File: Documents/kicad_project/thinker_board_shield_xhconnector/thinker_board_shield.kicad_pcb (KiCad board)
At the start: 4 copper layers, 56 x 65 mm, 8 parts, among them J2 Thinker_board_S, U1 XH_S, U2 1PIN, U3 XH_4PIN

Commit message: add big wire /before auto-router
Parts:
- added U4: 2_pin, hoshina_library:2_pin, B.Cu at (40.6, 8.89)
- moved R1 5.79 mm to (27.8, 9.53)
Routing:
- net GND: track 73.9 -> 52.2 mm, vias 2 -> 1
- net +3V3: track 27.5 -> 9.54 mm
- net Net-(U2-Pad1): track 13.1 -> 0.00 mm, vias 1 -> 0
- net Net-(R1-Pad1): track 4.20 -> 0.00 mm
- net 5V: track 90.1 -> 87.7 mm
- removed copper zone on B.Cu, net GND
- removed copper zone on F.Cu, net GND
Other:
- board text added: "3.3V"
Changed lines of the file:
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@@
   (general
     (thickness 1.6)
-    (drawings 18)
-    (tracks 49)
+    (drawings 20)
+    (tracks 27)
     (zones 0)
-    (modules 8)
+    (modules 9)
     (nets 36)
   )
@@
   )
   (setup
-    (last_trace_width 0.16)
+    (last_trace_width 1)
     (user_trace_width 0.16)
     (user_trace_width 0.2)
@@
   )
   (module hoshina_library:register_0603 (layer F.Cu)
-    (at 29.718 14.986)
+    (at 27.79 9.525)
     (descr aitendo_R0603-1)
     (tags capacitor)
@@
     (pad "" np_thru_hole circle (at 0 0) (size 2.7 2.7) (drill 2.7) (layers *.Cu *.Mask))
   )
+  (module hoshina_library:2_pin (layer B.Cu)
+    (at 40.64 8.89 180)
+    (fp_text reference U4 (at 0 -3.675) (layer B.SilkS)
+      (effects (font (size 1 1) (thickness 0.15)) (justify mirror))
+    )
+    (fp_text value 2_pin (at 0 -2.675) (layer B.Fab)
+      (effects (font (size 1 1) (thickness 0.15)) (justify mirror))
+    )
+    (fp_line (start -2.54 1.27) (end 2.54 1.27) (layer B.CrtYd) (width 0.12))
+    (fp_line (start 2.54 1.27) (end 2.54 -1.27) (layer B.CrtYd) (width 0.12))
+    (fp_line (start 2.54 -1.27) (end -2.54 -1.27) (layer B.CrtYd) (width 0.12))
+    (fp_line (start -2.54 -1.27) (end -2.54 1.27) (layer B.CrtYd) (width 0.12))
+    (fp_line (start -1.397 1.524) (end -1.397 5.842) (layer B.Fab) (width 0.12))
+    (fp_line (start -1.397 5.842) (end -1.143 5.842) (layer B.Fab) (width 0.12))
+    (fp_line (start -1.143 5.842) (end -1.143 1.524) (layer B.Fab) (width 0.12))
+    (fp_line (start 1.143 1.524) (end 1.143 5.842) (layer B.Fab) (width 0.12))
+    (fp_line (start 1.397 5.842) (end 1.397 1.524) (layer B.Fab) (width 0.12))
+    (fp_line (start 1.143 5.842) (end 1.397 5.842) (layer B.Fab) (width 0.12))
+    (pad 1 thru_hole circle (at -1.27 0 180) (size 1.524 1.524) (drill 0.762) (layers *.Cu *.Mask)
+      (net 33 +3V3))
+    (pad 2 thru_hole circle (at 1.27 0 180) (size 1.524 1.524) (drill 0.762) (layers *.Cu *.Mask)
+      (net 32 GND))
+  )
+  (gr_text GND (at 39.37 1.27 90) (layer B.SilkS)
+    (effects (font (size 0.5 0.5) (thickness 0.1)) (justify mirror))
+  )
+  (gr_text 3.3V (at 41.91 1.27 90) (layer B.SilkS)
+    (effects (font (size 0.5 0.5) (thickness 0.1)) (justify mirror))
+  )
   (gr_arc (start 47 17.7) (end 48 17.7) (angle -90) (layer Edge.Cuts) (width 0.15))
   (gr_text sw2 (at 32.512 1.016 90) (layer B.SilkS)
@@
   (gr_line (start 0 3.5) (end 0 15.7) (layer Edge.Cuts) (width 0.15))
   (gr_line (start 3.5 0) (end 52.5 0) (layer Edge.Cuts) (width 0.15))
-  (segment (start 53.77 8.37) (end 53.77 7.5) (width 1.5) (layer B.Cu) (net 31))
-  (segment (start 53.77 7.5) (end 52.84 6.57) (width 1.5) (layer B.Cu) (net 31))
-  (segment (start 52.84 6.57) (end 41.4862 6.57) (width 1.5) (layer B.Cu) (net 31))
-  (segment (start 41.4862 6.57) (end 40.0742 5.158) (width 1.5) (layer B.Cu) (net 31))
-  (segment (start 40.0742 5.158) (end 18.342 5.158) (width 1.5) (layer B.Cu) (net 31))
-  (segment (start 18.342 5.158) (end 13 10.5) (width 1.5) (layer B.Cu) (net 31))
-  (segment (start 53.77 8.37) (end 53.77 7.1679) (width 1.5) (layer F.Cu) (net 31))
-  (segment (start 53.77 7.1679) (end 53.1721 6.57) (width 1.5) (layer F.Cu) (net 31))
-  (segment (start 53.1721 6.57) (end 41.7238 6.57) (width 1.5) (layer F.Cu) (net 31))
-  (segment (start 41.7238 6.57) (end 40.0578 4.904) (width 1.5) (layer F.Cu) (net 31))
-  (segment (start 40.0578 4.904) (end 18.596 4.904) (width 1.5) (layer F.Cu) (net 31))
-  (segment (start 18.596 4.904) (end 13 10.5) (width 1.5) (layer F.Cu) (net 31))
-  (segment (start 45.512 13) (end 45.7496 13) (width 1.5) (layer B.Cu) (net 32))
-  (segment (start 45.7496 13) (end 45.8388 13.0892) (width 1.5) (layer B.Cu) (net 32))
-  (segment (start 49.025 16.2754) (end 49.025 17.5271) (width 1.5) (layer B.Cu) (net 32))
-  (segment (start 49.025 17.5271) (end 50.0279 18.53) (width 1.5) (layer B.Cu) (net 32))
-  (segment (start 50.0279 18.53) (end 51.23 18.53) (width 1.5) (layer B.Cu) (net 32))
-  (segment (start 51.23 18.53) (end 50.0279 18.53) (width 1.5) (layer F.Cu) (net 32))
-  (segment (start 50.0279 18.53) (end 49.025 17.5271) (width 1.5) (layer F.Cu) (net 32))
-  (segment (start 49.025 17.5271) (end 49.025 16.2754) (width 1.5) (layer F.Cu) (net 32))
-  (segment (start 14.2728 13) (end 13 13) (width 1.5) (layer F.Cu) (net 32))
-  (segment (start 32.5 12.689) (end 32.5 11.5) (width 0.2) (layer F.Cu) (net 32))
-  (segment (start 30.203 14.986) (end 32.5 12.689) (width 0.2) (layer F.Cu) (net 32))
-  (segment (start 45.7496 13) (end 41.194 13) (width 3) (layer B.Cu) (net 32))
-  (segment (start 36.576 8.382) (end 20.574 8.382) (width 3) (layer B.Cu) (net 32))
-  (segment (start 13 13) (end 14.686 13) (width 1.5) (layer B.Cu) (net 32))
-  (segment (start 19.304 8.382) (end 14.686 13) (width 1.5) (layer B.Cu) (net 32))
-  (segment (start 20.574 8.382) (end 19.304 8.382) (width 1.5) (layer B.Cu) (net 32))
-  (segment (start 20.574 8.382) (end 20.574 8.382) (width 3) (layer B.Cu) (net 32))
-  (via (at 20.574 8.382) (size 0.4) (drill 0.2) (layers F.Cu B.Cu) (net 32))
-  (segment (start 18.8908 8.382) (end 14.2728 13) (width 1.5) (layer F.Cu) (net 32))
-  (segment (start 20.574 8.382) (end 18.8908 8.382) (width 1.5) (layer F.Cu) (net 32))
-  (segment (start 45.8388 13.0892) (end 49.025 16.2754) (width 1.5) (layer B.Cu) (net 32))
-  (via (at 45.8388 13.0892) (size 0.4) (drill 0.2) (layers F.Cu B.Cu) (net 32))
-  (segment (start 49.025 16.2754) (end 45.8388 13.0892) (width 1.5) (layer F.Cu) (net 32))
-  (segment (start 34.094 9.906) (end 32.5 11.5) (width 0.16) (layer B.Cu) (net 32))
-  (segment (start 38.1 9.906) (end 34.094 9.906) (width 0.16) (layer B.Cu) (net 32))
-  (segment (start 38.1 9.906) (end 36.576 8.382) (width 3) (layer B.Cu) (net 32))
-  (segment (start 41.194 13) (end 38.1 9.906) (width 3) (layer B.Cu) (net 32))
-  (segment (start 28.13 8.37) (end 51.23 8.37) (width 0.16) (layer F.Cu) (net 33))
-  (segment (start 25 11.5) (end 28.13 8.37) (width 0.16) (layer F.Cu) (net 33))
-  (segment (start 29.233 13.233) (end 27.5 11.5) (width 0.2) (layer F.Cu) (net 34))
-  (segment (start 29.233 14.986) (end 29.233 13.233) (width 0.2) (layer F.Cu) (net 34))
-  (segment (start 25.498 16.002) (end 22.606 16.002) (width 0.16) (layer B.Cu) (net 35))
-  (segment (start 30 11.5) (end 25.498 16.002) (width 0.16) (layer B.Cu) (net 35))
-  (segment (start 22.606 16.002) (end 22.606 16.002) (width 0.16) (layer B.Cu) (net 35))
-  (via (at 22.606 16.002) (size 0.4) (drill 0.2) (layers F.Cu B.Cu) (net 35))
-  (segment (start 20.066 13.462) (end 19.812 13.462) (width 0.16) (layer F.Cu) (net 35))
-  (segment (start 22.606 16.002) (end 20.066 13.462) (width 0.16) (layer F.Cu) (net 35))
-  (zone (net 32) (net_name GND) (layer F.Cu) (hatch edge 0.508)
-    (connect_pads (clearance 0.2))
-    (min_thickness 0.254)
-    (fill yes (arc_segments 32) (thermal_gap 0.508) (thermal_bridge_width 0.508))
-    (polygon
-      (pts
-        (xy 0 0) (xy 58.42 0) (xy 58.42 68.58) (xy 0 68.58)
-      )
-    )
-  )
-  (zone (net 32) (net_name GND) (layer B.Cu) (hatch edge 0.508)
-    (connect_pads (clearance 0.2))
-    (min_thickness 0.254)
-    (fill yes (arc_segments 32) (thermal_gap 0.508) (thermal_bridge_width 0.508))
-    (polygon
-      (pts
-        (xy 0 -0.352342) (xy 58.42 -0.352342) (xy 58.42 68.227658) (xy 0 68.227658)
-      )
-    )
-  )
+  (segment (start 53.77 7.167919) (end 53.77 8.37) (width 1.5) (layer F.Cu) (net 31))
+  (segment (start 53.17208 6.569999) (end 53.77 7.167919) (width 1.5) (layer F.Cu) (net 31))
+  (segment (start 13 10.5) (end 16.930001 6.569999) (width 1.5) (layer F.Cu) (net 31))
+  (segment (start 16.930001 6.569999) (end 53.17208 6.569999) (width 1.5) (layer F.Cu) (net 31))
+  (segment (start 13.899999 9.600001) (end 13 10.5) (width 1.5) (layer B.Cu) (net 31))
+  (segment (start 16.930001 6.569999) (end 13.899999 9.600001) (width 1.5) (layer B.Cu) (net 31))
+  (segment (start 53.17208 6.569999) (end 16.930001 6.569999) (width 1.5) (layer B.Cu) (net 31))
+  (segment (start 53.77 8.37) (end 53.77 7.167919) (width 1.5) (layer B.Cu) (net 31))
+  (segment (start 53.77 7.167919) (end 53.17208 6.569999) (width 1.5) (layer B.Cu) (net 31))
+  (segment (start 48.148748 14.92499) (end 48.148748 14.92499) (width 3) (layer F.Cu) (net 32))
+  (via (at 48.148748 14.92499) (size 0.4) (drill 0.2) (layers F.Cu B.Cu) (net 32))
+  (segment (start 50.380001 17.680001) (end 51.23 18.53) (width 1.5) (layer F.Cu) (net 32))
+  (segment (start 50.255999 17.680001) (end 50.380001 17.680001) (width 1.5) (layer F.Cu) (net 32))
+  (segment (start 48.148748 14.92499) (end 48.148748 15.57275) (width 1.5) (layer F.Cu) (net 32))
+  (segment (start 48.148748 15.57275) (end 50.255999 17.680001) (width 1.5) (layer F.Cu) (net 32))
+  (segment (start 50.380001 17.680001) (end 51.23 18.53) (width 1.5) (layer B.Cu) (net 32))
+  (segment (start 50.255999 17.680001) (end 50.380001 17.680001) (width 1.5) (layer B.Cu) (net 32))
+  (segment (start 48.148748 14.92499) (end 48.148748 15.57275) (width 1.5) (layer B.Cu) (net 32))
+  (segment (start 48.148748 15.57275) (end 50.255999 17.680001) (width 1.5) (layer B.Cu) (net 32))
+  (segment (start 13.100001 13.100001) (end 13 13.100001) (width 3) (layer F.Cu) (net 32))
+  (segment (start 14.92499 14.92499) (end 13.100001 13.100001) (width 3) (layer F.Cu) (net 32))
+  (segment (start 39.37 13.97) (end 38.41501 14.92499) (width 1) (layer F.Cu) (net 32))
+  (segment (start 39.37 8.89) (end 39.37 13.97) (width 1) (layer F.Cu) (net 32))
+  (segment (start 48.148748 14.92499) (end 38.41501 14.92499) (width 3) (layer F.Cu) (net 32))
+  (segment (start 38.41501 14.92499) (end 14.92499 14.92499) (width 3) (layer F.Cu) (net 32))
+  (segment (start 50.71 8.89) (end 51.23 8.37) (width 1) (layer F.Cu) (net 33))
+  (segment (start 41.91 8.89) (end 50.71 8.89) (width 1) (layer F.Cu) (net 33))
 )

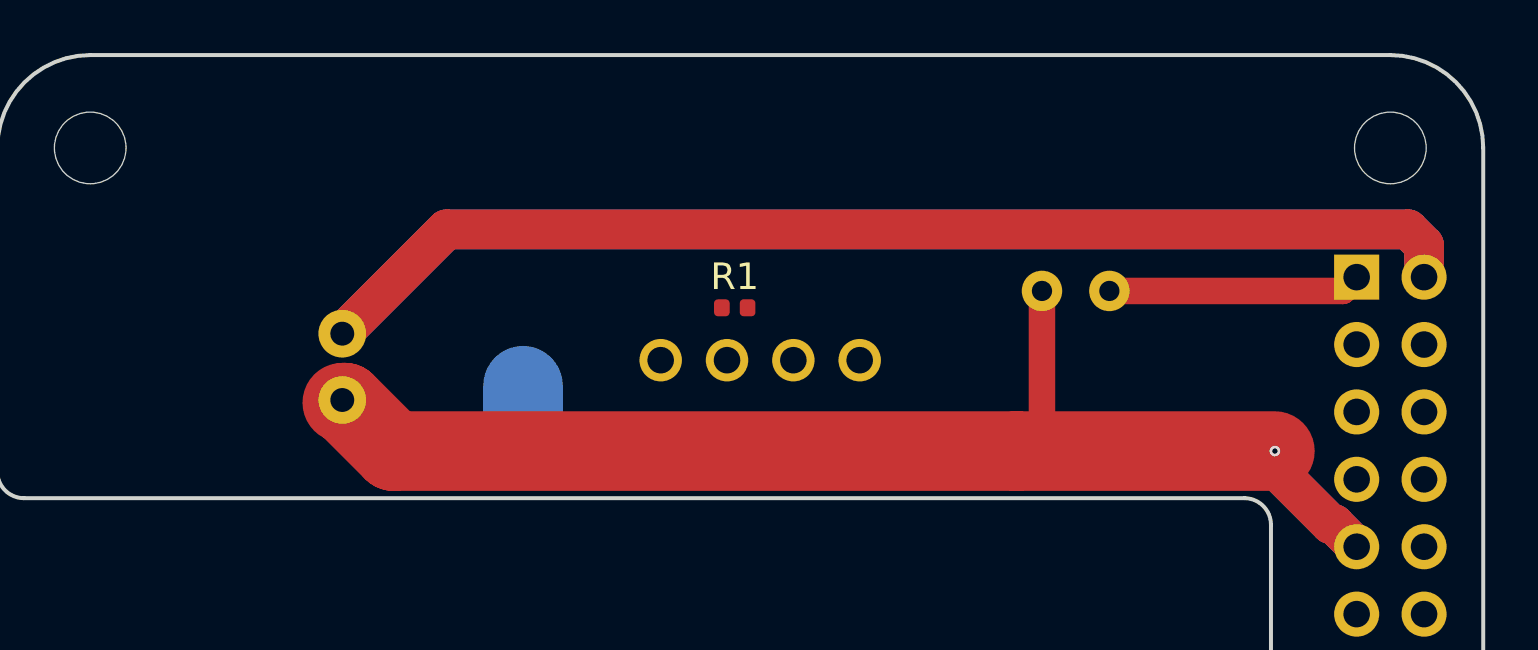
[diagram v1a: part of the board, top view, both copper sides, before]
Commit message: add parts and set position
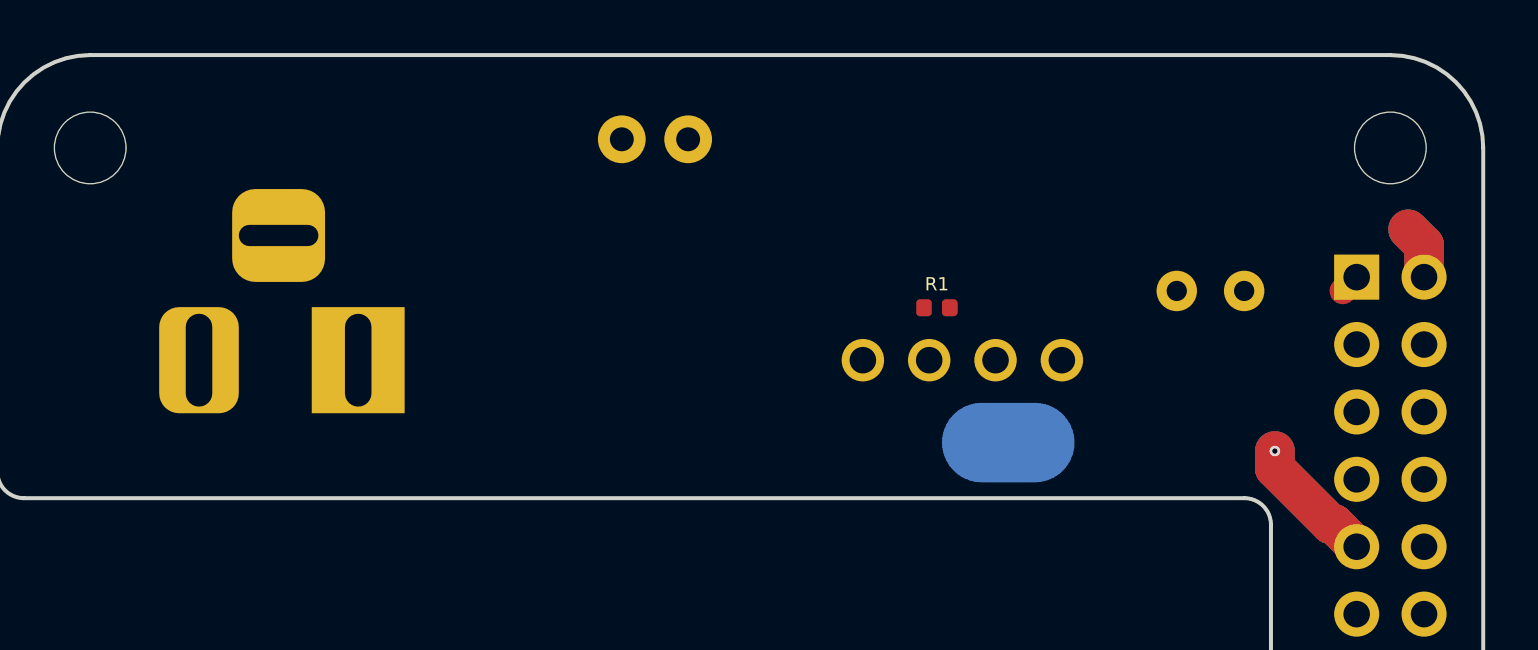
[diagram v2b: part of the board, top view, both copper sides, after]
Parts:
- added J1: Jack-DC, hoshina_library:DCJ, B.Cu at (13.6, 11.5)
- moved U2 18.3 mm to (38.1, 14.6), turned to 270 degrees
- moved U1 16.3 mm to (26.0, 3.17), turned to 270 degrees
- moved R1 7.62 mm to (35.4, 9.53)
- moved U3 7.62 mm to (32.6, 11.5)
- moved U4 5.08 mm to (45.7, 8.89)
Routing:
- net 5V: track 87.7 -> 4.10 mm
- net GND: track 52.2 -> 9.91 mm
- net +3V3: track 9.54 -> 0.74 mm
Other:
- board text added: "3V3"
- board text added: "fan"
- board text added: "power in"
- board text added: "power switch"
- board text added: "reset_pin"
- board text removed: "3.3V"

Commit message: make big wire /before auto-wire
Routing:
- net 5V: track 4.10 -> 63.3 mm, vias 0 -> 2
- net GND: track 9.91 -> 65.9 mm
- net +3V3: track 0.74 -> 5.19 mm
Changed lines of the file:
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@@
     (thickness 1.6)
     (drawings 24)
-    (tracks 15)
+    (tracks 44)
     (zones 0)
     (modules 10)
@@
   )
   (setup
-    (last_trace_width 0.15)
+    (last_trace_width 1)
     (user_trace_width 0.16)
     (user_trace_width 0.2)
@@
   (segment (start 53.77 8.37) (end 53.77 7.167919) (width 1.5) (layer B.Cu) (net 31))
   (segment (start 53.77 7.167919) (end 53.17208 6.569999) (width 1.5) (layer B.Cu) (net 31))
+  (segment (start 53.17208 6.569999) (end 50.765999 6.569999) (width 1.5) (layer B.Cu) (net 31))
+  (segment (start 50.765999 6.569999) (end 49.784 5.588) (width 1.5) (layer B.Cu) (net 31))
+  (segment (start 49.784 5.588) (end 49.784 5.588) (width 1.5) (layer B.Cu) (net 31))
+  (via (at 49.784 5.588) (size 0.4) (drill 0.2) (layers F.Cu B.Cu) (net 31))
+  (segment (start 49.784 5.588) (end 49.784 5.588) (width 1.5) (layer B.Cu) (net 31))
+  (via (at 49.784 5.588) (size 0.4) (drill 0.2) (layers F.Cu B.Cu) (net 31))
+  (segment (start 50.765999 6.569999) (end 49.784 5.588) (width 1.5) (layer F.Cu) (net 31))
+  (segment (start 53.17208 6.569999) (end 50.765999 6.569999) (width 1.5) (layer F.Cu) (net 31))
+  (segment (start 24.799997 5.787999) (end 49.584001 5.787999) (width 3) (layer B.Cu) (net 31))
+  (segment (start 23.434999 4.423001) (end 24.799997 5.787999) (width 3) (layer B.Cu) (net 31))
+  (segment (start 23.434999 3.275001) (end 23.434999 4.423001) (width 3) (layer B.Cu) (net 31))
+  (segment (start 23.36001 3.34999) (end 23.434999 3.275001) (width 3) (layer B.Cu) (net 31))
+  (segment (start 8.658394 3.34999) (end 23.36001 3.34999) (width 3) (layer B.Cu) (net 31))
+  (segment (start 7.14999 4.858394) (end 8.658394 3.34999) (width 3) (layer B.Cu) (net 31))
+  (segment (start 7.14999 8.94999) (end 7.14999 4.858394) (width 3) (layer B.Cu) (net 31))
+  (segment (start 7.6 9.4) (end 7.14999 8.94999) (width 3) (layer B.Cu) (net 31))
+  (segment (start 7.6 11.5) (end 7.6 9.4) (width 3) (layer B.Cu) (net 31))
   (segment (start 48.148748 14.92499) (end 48.148748 14.92499) (width 3) (layer F.Cu) (net 32))
   (via (at 48.148748 14.92499) (size 0.4) (drill 0.2) (layers F.Cu B.Cu) (net 32))
@@
   (segment (start 48.148748 14.92499) (end 48.148748 15.57275) (width 1.5) (layer B.Cu) (net 32))
   (segment (start 48.148748 15.57275) (end 50.255999 17.680001) (width 1.5) (layer B.Cu) (net 32))
+  (segment (start 47.865906 14.92499) (end 48.148748 14.92499) (width 3) (layer F.Cu) (net 32))
+  (segment (start 13.6 11.5) (end 18.35 11.5) (width 3) (layer F.Cu) (net 32))
+  (segment (start 18.35 11.5) (end 21.77499 14.92499) (width 3) (layer F.Cu) (net 32))
+  (segment (start 26.135001 3.275001) (end 26.135001 3.175) (width 3) (layer F.Cu) (net 32))
+  (segment (start 28.13299 5.27299) (end 26.135001 3.275001) (width 3) (layer F.Cu) (net 32))
+  (segment (start 28.13299 14.92499) (end 28.13299 5.27299) (width 3) (layer F.Cu) (net 32))
+  (segment (start 28.13299 14.92499) (end 47.865906 14.92499) (width 3) (layer F.Cu) (net 32))
+  (segment (start 21.77499 14.92499) (end 28.13299 14.92499) (width 3) (layer F.Cu) (net 32))
+  (segment (start 44.45 11.509084) (end 47.865906 14.92499) (width 1) (layer F.Cu) (net 32))
+  (segment (start 44.45 8.89) (end 44.45 11.509084) (width 1) (layer F.Cu) (net 32))
   (segment (start 50.71 8.89) (end 51.23 8.37) (width 1) (layer F.Cu) (net 33))
+  (segment (start 47.51 8.37) (end 46.99 8.89) (width 1) (layer F.Cu) (net 33))
+  (segment (start 51.23 8.37) (end 47.51 8.37) (width 1) (layer F.Cu) (net 33))
 )

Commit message: change to raspi
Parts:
- added s1: connectable_smd, hoshina_library:connectable_smd, F.Cu at (35.5, 6.35)
- added s2: connectable_smd, hoshina_library:connectable_smd, F.Cu at (32.9, 6.35)
- added s3: connectable_smd, hoshina_library:connectable_smd, F.Cu at (29.2, 6.35)
- added s4: connectable_smd, hoshina_library:connectable_smd, F.Cu at (38.1, 6.35)
- moved U4 5.10 mm to (43.5, 13.5)
- moved U2 3.80 mm to (34.3, 15.0)
- moved U1 3.67 mm to (22.6, 4.57)
- moved R1 3.27 mm to (32.1, 9.53)
- moved U3 3.27 mm to (29.4, 11.5)
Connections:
- J2 pad 37: Net-(J2-Pad37) -> Raspi_GPIO26
- J2 pad 40: Net-(J2-Pad40) -> Raspi_SCL
- J2 pad 8: Net-(J2-Pad8) -> Raspi_TX
- U3 pad 1: +3V3 -> Net-(U3-Pad1)
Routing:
- net GND: track 65.9 -> 0.00 mm, vias 1 -> 0
- net 5V: track 63.3 -> 0.00 mm, vias 2 -> 0
- net +3V3: track 5.19 -> 0.00 mm
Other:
- board text added: "Raspberry Pi"
- board text added: "Thinker Board"
- board text added: "power_in"
- board text added: "power_switch"
- board text added: "thinker_reset_pin"
- board text removed: "power in"
- board text removed: "power switch"
- board text removed: "reset_pin"
